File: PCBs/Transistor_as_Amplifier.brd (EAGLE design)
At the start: 38 x 26 mm, 12 parts, among them T1 BC547N

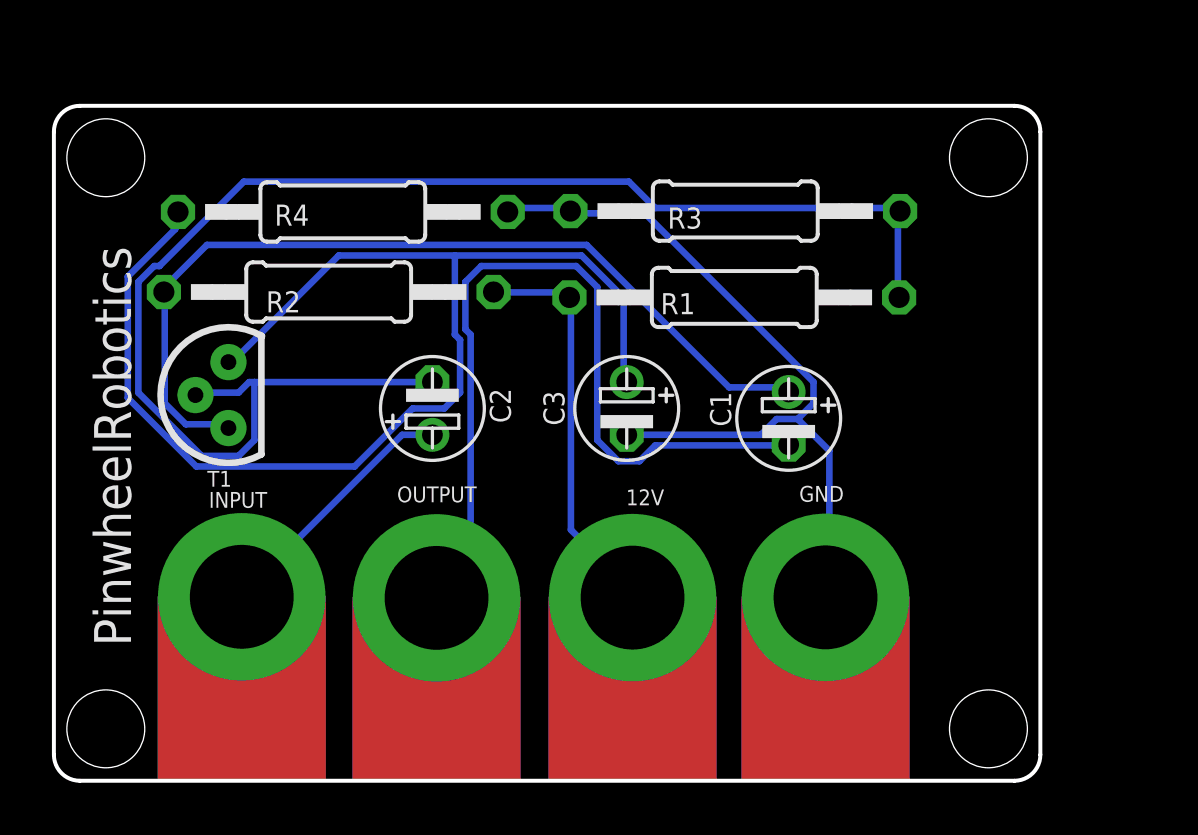
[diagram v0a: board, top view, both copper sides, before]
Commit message: Corrected dimesnion for
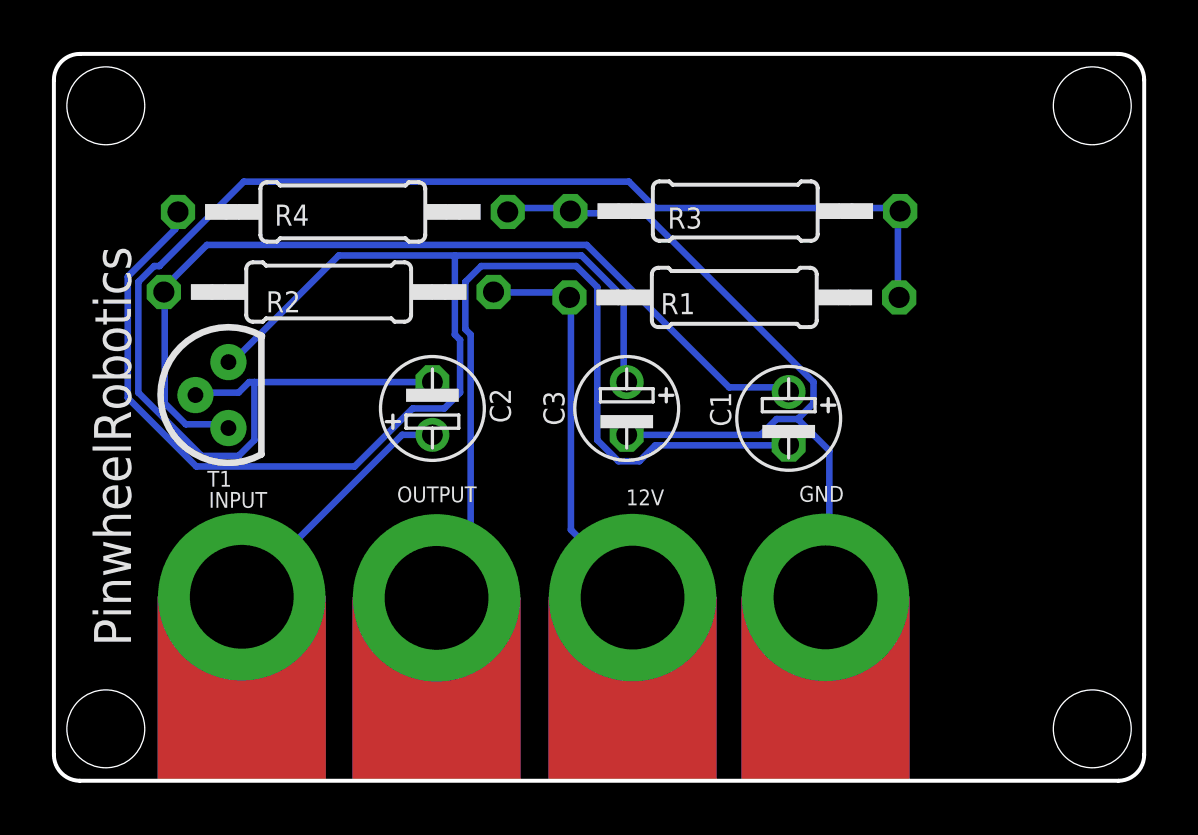
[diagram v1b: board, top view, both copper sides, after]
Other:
- board size 38 x 26 mm -> 42 x 28 mm
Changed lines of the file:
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@@
 <board>
 <plain>
-<hole x="2" y="24" drill="3"/>
+<hole x="2" y="26" drill="3"/>
 <hole x="2" y="2" drill="3"/>
-<hole x="36" y="2" drill="3"/>
-<hole x="36" y="24" drill="3"/>
+<hole x="40" y="2" drill="3"/>
+<hole x="40" y="26" drill="3"/>
 <text x="2.969753125" y="5.185003125" size="1.4224" layer="21" ratio="7" rot="R90">PinwheelRobotics </text>
 <text x="35.524521875" y="20.041015625" size="1.4224" layer="22" ratio="7" rot="MR270">care@pinwheel</text>
-<wire x1="37" y1="26" x2="1" y2="26" width="0.1524" layer="20"/>
-<wire x1="1" y1="26" x2="0" y2="25" width="0.1524" layer="20" curve="90"/>
-<wire x1="0" y1="25" x2="0" y2="1" width="0.1524" layer="20"/>
+<wire x1="41" y1="28" x2="1" y2="28" width="0.1524" layer="20"/>
+<wire x1="1" y1="28" x2="0" y2="27" width="0.1524" layer="20" curve="90"/>
+<wire x1="0" y1="27" x2="0" y2="1" width="0.1524" layer="20"/>
 <wire x1="0" y1="1" x2="1" y2="0" width="0.1524" layer="20" curve="90"/>
-<wire x1="1" y1="0" x2="37" y2="0" width="0.1524" layer="20"/>
-<wire x1="37" y1="0" x2="38" y2="1" width="0.1524" layer="20" curve="90"/>
-<wire x1="38" y1="1" x2="38" y2="25" width="0.1524" layer="20"/>
-<wire x1="38" y1="25" x2="37" y2="26" width="0.1524" layer="20" curve="90"/>
-<dimension x1="-1.5" y1="26" x2="-1.5" y2="0" x3="-3" y3="13" textsize="1.778" layer="1"/>
-<dimension x1="0" y1="26.5" x2="38" y2="26.5" x3="19" y3="28.5" textsize="1.778" layer="1"/>
+<wire x1="1" y1="0" x2="41" y2="0" width="0.1524" layer="20"/>
+<wire x1="41" y1="0" x2="42" y2="1" width="0.1524" layer="20" curve="90"/>
+<wire x1="42" y1="1" x2="42" y2="27" width="0.1524" layer="20"/>
+<wire x1="42" y1="27" x2="41" y2="28" width="0.1524" layer="20" curve="90"/>
+<dimension x1="-1.5" y1="0" x2="-1.5" y2="28" x3="-2.5" y3="14" textsize="1.778" layer="1"/>
+<dimension x1="0" y1="29" x2="42" y2="29" x3="21" y3="29.5" textsize="1.778" layer="1"/>
+<dimension x1="2" y1="24" x2="40" y2="24" x3="21" y3="32" textsize="1.778" layer="1"/>
+<dimension x1="0.5" y1="26" x2="0.5" y2="2" x3="-5.5" y3="14" textsize="1.778" layer="1"/>
 </plain>
 <attributes>

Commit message: Corrected hole position for some design , made transistor as switch as category 1
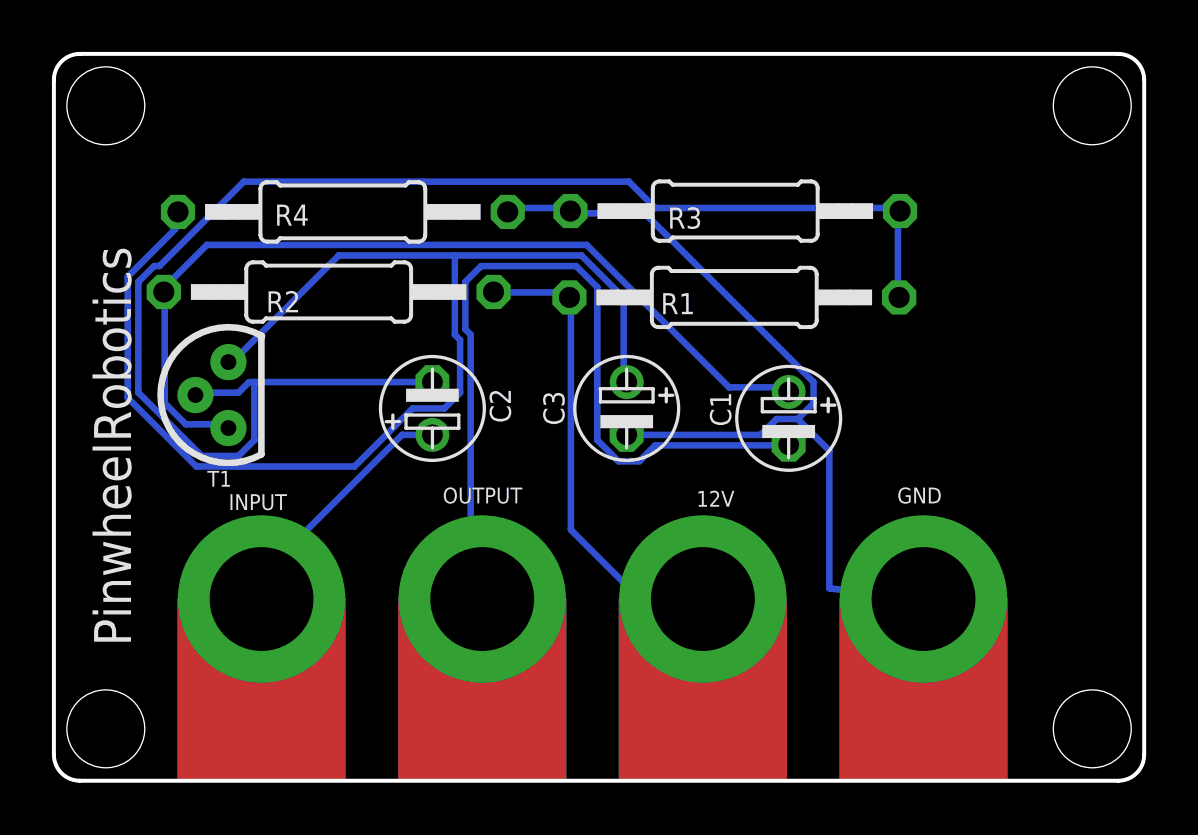
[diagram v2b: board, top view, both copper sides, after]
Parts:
- moved GND 3.78 mm to (33.5, 7.00)
- moved 12V 2.71 mm to (25.0, 7.00)
- moved OUTPUT 1.76 mm to (16.5, 7.00)
- moved INPUT 0.77 mm to (8.00, 7.00)
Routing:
- net GND: track 30.5 -> 33.8 mm
- net 12V: track 15.6 -> 18.1 mm
- net N$4: track 32.4 -> 33.9 mm
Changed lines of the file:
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@@
 </autorouter>
 <elements>
-<element name="12V" library="microbit" package="MICROBIT_PAD" value="MICROBIT_PAD" x="22.291428125" y="7.055215625" smashed="yes">
-<attribute name="NAME" x="22.037428125" y="10.611215625" size="0.6096" layer="21" font="vector"/>
+<element name="12V" library="microbit" package="MICROBIT_PAD" value="MICROBIT_PAD" x="25" y="7" smashed="yes">
+<attribute name="NAME" x="24.746" y="10.556" size="0.6096" layer="21" font="vector"/>
 </element>
 <element name="C1" library="we-rcl" package="C_E2-4" value="10uF" x="28.3052875" y="13.960615625" smashed="yes">
@@
 <attribute name="VALUE" x="24.6062875" y="14.341615625" size="0.8128" layer="27" font="vector" ratio="10" rot="R270" align="center"/>
 </element>
-<element name="GND" library="microbit" package="MICROBIT_PAD" value="MICROBIT_PAD" x="29.72461875" y="7.064284375" smashed="yes">
-<attribute name="NAME" x="28.70861875" y="10.747284375" size="0.6096" layer="21" font="vector"/>
+<element name="GND" library="microbit" package="MICROBIT_PAD" value="MICROBIT_PAD" x="33.5" y="7" smashed="yes">
+<attribute name="NAME" x="32.484" y="10.683" size="0.6096" layer="21" font="vector"/>
 </element>
-<element name="INPUT" library="microbit" package="MICROBIT_PAD" value="MICROBIT_PAD" x="7.23673125" y="7.08611875" smashed="yes">
-<attribute name="NAME" x="5.96673125" y="10.51511875" size="0.6096" layer="21" font="vector"/>
+<element name="INPUT" library="microbit" package="MICROBIT_PAD" value="MICROBIT_PAD" x="8" y="7" smashed="yes">
+<attribute name="NAME" x="6.73" y="10.429" size="0.6096" layer="21" font="vector"/>
 </element>
-<element name="OUTPUT" library="microbit" package="MICROBIT_PAD" value="MICROBIT_PAD" x="14.741034375" y="7.044221875" smashed="yes">
-<attribute name="NAME" x="13.217034375" y="10.727221875" size="0.6096" layer="21" font="vector"/>
+<element name="OUTPUT" library="microbit" package="MICROBIT_PAD" value="MICROBIT_PAD" x="16.5" y="7" smashed="yes">
+<attribute name="NAME" x="14.976" y="10.683" size="0.6096" layer="21" font="vector"/>
 </element>
 <element name="R1" library="rcl" library_urn="urn:adsk.eagle:library:334" package="0207/12" package3d_urn="urn:adsk.eagle:package:23489/1" value="100k" x="26.209478125" y="18.6192" smashed="yes" rot="R180">
@@
 <wire x1="14.85309375" y1="7.044221875" x2="16.0544875" y2="8.245615625" width="0.254" layer="16"/>
 <wire x1="28.2464875" y1="12.919215625" x2="28.3052875" y2="12.944615625" width="0.254" layer="16"/>
-<wire x1="14.85309375" y1="7.044221875" x2="14.741034375" y2="7.044221875" width="0.254" layer="16"/>
+<wire x1="14.85309375" y1="7.044221875" x2="16.5" y2="7" width="0.254" layer="16"/>
 </signal>
 <signal name="N$7">
@@
 <wire x1="13.4128875" y1="13.325615625" x2="14.5812875" y2="13.325615625" width="0.254" layer="16"/>
 <wire x1="8.016821875" y1="7.92955" x2="13.4128875" y2="13.325615625" width="0.254" layer="16"/>
-<wire x1="8.016821875" y1="7.92955" x2="7.23673125" y2="7.08611875" width="0.254" layer="16"/>
+<wire x1="8.016821875" y1="7.92955" x2="8" y2="7" width="0.254" layer="16"/>
 </signal>
 <signal name="12V">
@@
 <wire x1="22.204034375" y1="7.37926875" x2="19.9152875" y2="9.668015625" width="0.254" layer="16"/>
 <wire x1="19.9152875" y1="18.608815625" x2="19.859478125" y2="18.6192" width="0.254" layer="16"/>
-<wire x1="22.204034375" y1="7.37926875" x2="22.291428125" y2="7.055215625" width="0.254" layer="16"/>
+<wire x1="22.204034375" y1="7.37926875" x2="25" y2="7" width="0.254" layer="16"/>
 </signal>
 <signal name="GND">
@@
 <wire x1="29.8720875" y1="12.716015625" x2="28.6528875" y2="13.935215625" width="0.254" layer="16"/>
 <wire x1="29.8720875" y1="7.410121875" x2="29.8720875" y2="12.716015625" width="0.254" layer="16"/>
-<wire x1="29.8720875" y1="7.410121875" x2="29.72461875" y2="7.064284375" width="0.254" layer="16"/>
+<wire x1="29.8720875" y1="7.410121875" x2="33.5" y2="7" width="0.254" layer="16"/>
 <wire x1="22.7600875" y1="21.860015625" x2="19.9152875" y2="21.860015625" width="0.254" layer="16"/>
 <wire x1="29.2624875" y1="15.357615625" x2="22.7600875" y2="21.860015625" width="0.254" layer="16"/>
